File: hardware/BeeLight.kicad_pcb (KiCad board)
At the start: 2 copper layers, 32 x 24 mm, 23 parts, among them IC102 APDS-9306-065, IC103 BME688, M101 BL54L15, Q101 BSS84, SW101 JOIN, X102 DEBUG

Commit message: Hardware rev 1 seems to be working
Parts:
- moved R105 0.76 mm to (128.0, 87.2), turned to 180 degrees
- moved IC102 0.30 mm to (125.6, 88.4)
- moved R106 0.29 mm to (124.3, 90.6)
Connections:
- M101 pad 31: unconnected-(M101-P0.04-Pad31) -> SDA
- M101 pad 38: SDA -> unconnected-(M101-P2.06-Pad38)
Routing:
- net SDA: track 22.4 -> 23.1 mm

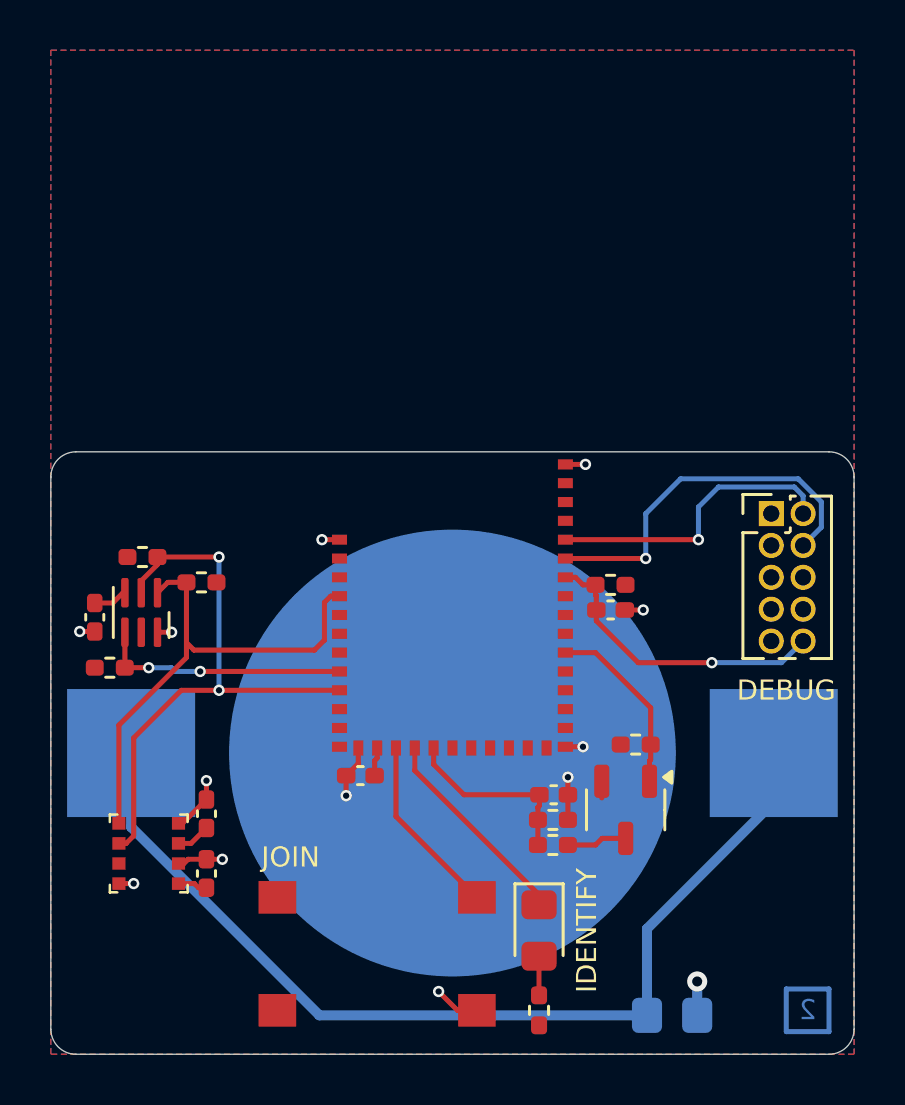
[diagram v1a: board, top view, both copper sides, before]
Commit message: Bring up hardware and firmware
- Remove old files

- Update README.md
- Update converter for z2m

- Fix typos in DTS includes
- Fix wrong patch command

- Add dimension to PCB specification Kibot output
- Add blocklist to west.yml
- Add missing mounting holes
- Add custom cluster for VOC, IAQ and CO2 for Zigbee2Mqtt
- Add patches for custom cluster for ncs-zigbee
- Add west command to build and flash the device configuration
- Add 3D files for the housing
- Add 3D printer project for the housing
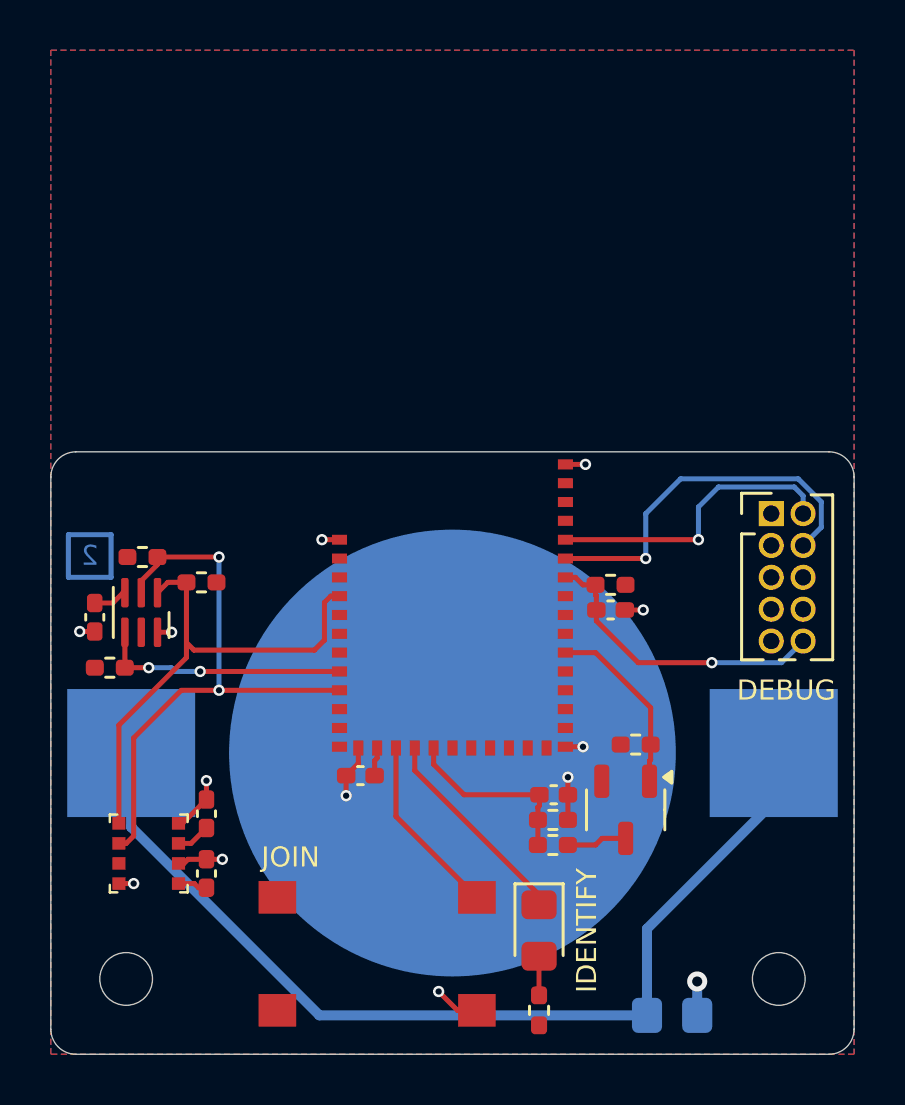
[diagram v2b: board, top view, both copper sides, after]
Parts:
- added REF**: MountingHole_2.1mm, MountingHole:MountingHole_2.1mm, F.Cu at (125.0, 103.0)
- added REF**: MountingHole_2.1mm, MountingHole:MountingHole_2.1mm, F.Cu at (151.0, 103.0)
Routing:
- net +BATT: track 7.19 -> 6.41 mm

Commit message: - Remove old files
- Replace nRF54 module

- Update README.md
- Update converter for z2m

- Fix typos in DTS includes
- Fix wrong patch command

- Add BME688
- Add dimension to PCB specification Kibot output
- Add blocklist to west.yml
- Add missing mounting holes
- Add custom cluster for VOC, IAQ and CO2 for Zigbee2Mqtt
- Add patches for custom cluster for ncs-zigbee
- Add west command to build and flash the device configuration
- Add 3D files for the housing
- Add 3D printer project for the housing
- Add template from Vincent
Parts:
- R108: value 8k2 / 0.1% -> 8k2
- R109: value 2k2 / 0.1% -> 2k2
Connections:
- net BAT_E renamed Enable-Battery
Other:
- board text added: "2"
- board text removed: "${REVISION}"

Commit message: - Change ADC filter capacitor to 1 nF - Update documentation with current consumption - Update CI/CD pipeline
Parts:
- C103: value 100n -> 1n
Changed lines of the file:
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@@
 		)
 	)
-	(property "ASSEMBLY_NOTES" "ASSEMBLY NOTES (UNLESS OTHERWISE SPECIFIED)\n\n1)	DO NOT POPULATE PARTS ARE MARKED WITH A RED CROSS.\n\n2)	DO NOT POPULATE PARTS ARE NOT PRESENT IN THE BOM.\n\n3)	IF CONFLICTING INFORMATION IS FOUND BETWEEN THE ASSEMBLY\n	FILE AND BOM, BOM SHOULD BE USED AS THE MAIN SOURCE.\n\n4)	CONFORMAL COATING IS NOT REQUIRED.\n\n5)	DOT IDENTIFIES PIN #1 LOCATION AND DEVICE ORIENTATION\n	WHEN VIEWED FROM THE TOP.")
+	(property "ASSEMBLY_NOTES" "")
 	(property "BOARD_NAME" "BeeLight")
 	(property "COMPANY" "null")
 	(property "DESIGNER" "Daniel Kampert")
-	(property "FABRICATION_NOTES" "FABRICATION NOTES (UNLESS OTHERWISE SPECIFIED)\n\n1)	FABRICATE PER IPC-6012A CLASS 2.\n\n2)	OUTLINE DEFINED IN SEPARATE GERBER FILE WITH\n	\"Edge_Cuts.GBR\" SUFFIX.\n\n	DIMENSIONS OF CIRCUMSIZED RECTANGLE SHOWN ON THIS\n	DRAWING FOR REFERENCE ONLY.\n\n3)	SEE SEPARATE DRILL FILES WITH \".DRL\" SUFFIX \n	FOR HOLE LOCATIONS.\n\n	SELECTED HOLE LOCATIONS SHOWN ON THIS DRAWING \n	FOR REFERENCE ONLY.\n\n4)	SURFACE FINISH: IMMERSION GOLD\n\n5)	SOLDERMASK ON BOTH SIDES OF THE BOARD SHALL \n	BE LPI, COLOR BLUE.\n\n6)	SILK SCREEN LEGEND TO BE APPLIED PER LAYER \n	STACKUP USING WHITE NON-CONDUCTIVE EPOXY INK.\n\n7)	ALL VIAS ARE TENTED ON BOTH SIDES UNLESS \n	SOLDERMASK OPENED IN GERBER.\n\n8)	VENDOR SHOULD FOLLOW ROHS COMPLIANT PROCESS \n	AND Pb FREE FOR MANUFACTURING\n\n9)	PCB MATERIAL REQUIREMENTS:\n\n	A.	FLAMMABILITY RATING MUST MEET OR EXCEED \n		UL94V-0 REQUIREMENTS.\n	B.	Tg 170 C OR EQUIVALENT.\n	C.	EQUIVALENT MATERIAL SHALL BE RoHS COMPLIANT, \n		HALOGEN FREE AND APPROVED BY NULL.\n\n10)	DESIGN GEOMETRY MINIMUM FEATURE SIZES:\n\n	BOARD SIZE				32.000 × 24.000 mm\n	BOARD THICKNESS		1.600 mm\n	TRACE WIDTH			0.200 mm\n	TRACE TO TRACE		0.125 mm\n	MIN. HOLE (PTH)			0.250 mm\n	MIN. HOLE (NPTH)		2.100 mm\n	ANNULAR RING			0.100 mm\n	COPPER TO HOLE		0.125 mm\n	COPPER TO EDGE		0.125 mm\n	HOLE TO HOLE			0.250 mm\n\n11)	REFER TO IMPEDANCE TABLE FOR IMPEDANCE CONTROL REQUIREMENTS.\n\n12)	CONFIRM SPACE WIDTHS AND SPACINGS.")
-	(property "GIT_HASH_PCB" "c0285d5")
-	(property "GIT_HASH_SCH" "c0285d5")
+	(property "FABRICATION_NOTES" "")
+	(property "GIT_HASH_PCB" "0c20f1f")
+	(property "GIT_HASH_SCH" "0c20f1f")
 	(property "GIT_URL" "https://github.com/Kampi/BeeLight")
 	(property "PROJECT_NAME" "BeeLight")
 	(property "RELEASE_BODY_UNRELEASED" "Version Unreleased not found.")
-	(property "RELEASE_DATE" "06-Jun-2025")
-	(property "RELEASE_DATE_NUM" "2025-06-06")
+	(property "RELEASE_DATE" "19-Jun-2025")
+	(property "RELEASE_DATE_NUM" "2025-06-19")
 	(property "RELEASE_TITLE_UNRELEASED" "Version Unreleased not found.")
-	(property "REVISION" "(Unreleased)")
+	(property "REVISION" "+ (Unreleased)")
 	(property "SHEET_NAME_1" "Cover Page")
-	(property "SHEET_NAME_10" "......................................")
-	(property "SHEET_NAME_11" "......................................")
-	(property "SHEET_NAME_12" "......................................")
-	(property "SHEET_NAME_13" "......................................")
-	(property "SHEET_NAME_14" "......................................")
-	(property "SHEET_NAME_15" "......................................")
-	(property "SHEET_NAME_16" "......................................")
-	(property "SHEET_NAME_17" "......................................")
-	(property "SHEET_NAME_18" "......................................")
-	(property "SHEET_NAME_19" "......................................")
-	(property "SHEET_NAME_2" "Block Diagram")
-	(property "SHEET_NAME_20" "......................................")
-	(property "SHEET_NAME_21" "......................................")
-	(property "SHEET_NAME_22" "......................................")
-	(property "SHEET_NAME_23" "......................................")
-	(property "SHEET_NAME_24" "......................................")
-	(property "SHEET_NAME_25" "......................................")
-	(property "SHEET_NAME_26" "......................................")
-	(property "SHEET_NAME_27" "......................................")
-	(property "SHEET_NAME_28" "......................................")
-	(property "SHEET_NAME_29" "......................................")
-	(property "SHEET_NAME_3" "Project Architecture")
-	(property "SHEET_NAME_30" "......................................")
-	(property "SHEET_NAME_31" "......................................")
-	(property "SHEET_NAME_32" "......................................")
-	(property "SHEET_NAME_33" "......................................")
-	(property "SHEET_NAME_34" "......................................")
-	(property "SHEET_NAME_35" "......................................")
-	(property "SHEET_NAME_36" "......................................")
-	(property "SHEET_NAME_37" "......................................")
-	(property "SHEET_NAME_38" "......................................")
-	(property "SHEET_NAME_39" "......................................")
-	(property "SHEET_NAME_4" "Main")
-	(property "SHEET_NAME_40" "......................................")
-	(property "SHEET_NAME_5" "Revision History")
-	(property "SHEET_NAME_6" "......................................")
-	(property "SHEET_NAME_7" "......................................")
-	(property "SHEET_NAME_8" "......................................")
-	(property "SHEET_NAME_9" "......................................")
+	(property "SHEET_NAME_10" "Error: XML File not found")
+	(property "SHEET_NAME_11" "Error: XML File not found")
+	(property "SHEET_NAME_12" "Error: XML File not found")
+	(property "SHEET_NAME_13" "Error: XML File not found")
+	(property "SHEET_NAME_14" "Error: XML File not found")
+	(property "SHEET_NAME_15" "Error: XML File not found")
+	(property "SHEET_NAME_16" "Error: XML File not found")
+	(property "SHEET_NAME_17" "Error: XML File not found")
+	(property "SHEET_NAME_18" "Error: XML File not found")
+	(property "SHEET_NAME_19" "Error: XML File not found")
+	(property "SHEET_NAME_2" "Error: XML File not found")
+	(property "SHEET_NAME_20" "Error: XML File not found")
+	(property "SHEET_NAME_21" "Error: XML File not found")
+	(property "SHEET_NAME_22" "Error: XML File not found")
+	(property "SHEET_NAME_23" "Error: XML File not found")
+	(property "SHEET_NAME_24" "Error: XML File not found")
+	(property "SHEET_NAME_25" "Error: XML File not found")
+	(property "SHEET_NAME_26" "Error: XML File not found")
+	(property "SHEET_NAME_27" "Error: XML File not found")
+	(property "SHEET_NAME_28" "Error: XML File not found")
+	(property "SHEET_NAME_29" "Error: XML File not found")
+	(property "SHEET_NAME_3" "Error: XML File not found")
+	(property "SHEET_NAME_30" "Error: XML File not found")
+	(property "SHEET_NAME_31" "Error: XML File not found")
+	(property "SHEET_NAME_32" "Error: XML File not found")
+	(property "SHEET_NAME_33" "Error: XML File not found")
+	(property "SHEET_NAME_34" "Error: XML File not found")
+	(property "SHEET_NAME_35" "Error: XML File not found")
+	(property "SHEET_NAME_36" "Error: XML File not found")
+	(property "SHEET_NAME_37" "Error: XML File not found")
+	(property "SHEET_NAME_38" "Error: XML File not found")
+	(property "SHEET_NAME_39" "Error: XML File not found")
+	(property "SHEET_NAME_4" "Error: XML File not found")
+	(property "SHEET_NAME_40" "Error: XML File not found")
+	(property "SHEET_NAME_5" "Error: XML File not found")
+	(property "SHEET_NAME_6" "Error: XML File not found")
+	(property "SHEET_NAME_7" "Error: XML File not found")
+	(property "SHEET_NAME_8" "Error: XML File not found")
+	(property "SHEET_NAME_9" "Error: XML File not found")
 	(property "VARIANT" "PRELIMINARY")
 	(net 0 "")
@@
 			)
 		)
-		(property "Value" "100n"
+		(property "Value" "1n"
 			(at 0 1.16 0)
 			(layer "F.Fab")
@@
 			)
 		)
-		(property "Datasheet" "https://www.mouser.de/datasheet/2/40/KGM_X7R-3223212.pdf"
+		(property "Datasheet" "https://search.murata.co.jp/Ceramy/image/img/A01X/G101/ENG/GCM1555C2A102JE02-01A.pdf"
 			(at 0 0 0)
 			(unlocked yes)
@@
 			)
 		)
-		(property "manf" "KYOCERA AVX"
-			(at 0 0 0)
-			(unlocked yes)
-			(layer "F.Fab")
-			(hide yes)
-			(effects
-				(font
-					(size 0.8 0.8)
-					(thickness 0.12)
-				)
-			)
-		)
-		(property "manf#" "04025C104KAT4A"
-			(at 0 0 0)
-			(unlocked yes)
-			(layer "F.Fab")
-			(hide yes)
-			(effects
-				(font
-					(size 0.8 0.8)
-					(thickness 0.12)
-				)
-			)
-		)
-		(property "Distributor" "Mouser"
-			(at 0 0 0)
-			(unlocked yes)
-			(layer "F.Fab")
-			(hide yes)
-			(effects
-				(font
-					(size 0.8 0.8)
-					(thickness 0.12)
-				)
-			)
-		)
-		(property "mouser#" "581-04025C104KAT4A"
-			(at 0 0 0)
-			(unlocked yes)
+		(property "manf" "Murata Electronics"
+			(at 0 0 0)
+			(unlocked yes)
+			(layer "F.Fab")
+			(hide yes)
+			(effects
+				(font
+					(size 0.8 0.8)
+					(thickness 0.12)
+				)
+			)
+		)
+		(property "manf#" "GCM1555C2A102JE02D"
+			(at 0 0 0)
+			(unlocked yes)
+			(layer "F.Fab")
+			(hide yes)
+			(effects
+				(font
+					(size 0.8 0.8)
+					(thickness 0.12)
+				)
+			)
+		)
+		(property "mouser#" "81-GCM1555C2A102JE02D"
+			(at 0 0 0)
+			(unlocked yes)
+			(layer "F.Fab")
+			(hide yes)
+			(effects
+				(font
+					(size 0.8 0.8)
+					(thickness 0.12)
+				)
+			)
+		)
+		(property "CONFIG" ""
+			(at 0 0 0)
+			(unlocked yes)
